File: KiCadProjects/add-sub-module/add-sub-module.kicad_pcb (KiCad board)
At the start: 2 copper layers, 0 parts

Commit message: Finished add-sub schematic
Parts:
- added U1: CD74HCT10E, footprints.pretty3:N14, F.Cu at (127.2, 108.5)
- added U2: SN74HCT00N, footprints.pretty6:N14, F.Cu at (137.8, 108.5)
- added U3: SN74HCT02N, footprints.pretty7:N14, F.Cu at (148.3, 108.5)
- added U4: SN74HCT257N, footprints.pretty8:N16, F.Cu at (158.9, 109.8)
- added U5: CD74HCT04E, footprints.pretty1:N14, F.Cu at (169.5, 108.5)

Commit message: rev. v1 for add sub
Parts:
- added C1: 0.1 uF, Capacitor_THT:C_Disc_D4.7mm_W2.5mm_P5.00mm, F.Cu at (147.0, 68.5)
- added C2: 0.1 uF, Capacitor_THT:C_Disc_D4.7mm_W2.5mm_P5.00mm, F.Cu at (147.0, 73.5)
- added C3: 0.1 uF, Capacitor_THT:C_Disc_D4.7mm_W2.5mm_P5.00mm, F.Cu at (147.0, 78.5)
- added C4: 0.1 uF, Capacitor_THT:C_Disc_D4.7mm_W2.5mm_P5.00mm, F.Cu at (147.0, 115.5)
- added C5: 0.1 uF, Capacitor_THT:C_Disc_D4.7mm_W2.5mm_P5.00mm, F.Cu at (147.0, 120.5)
- added D1: D, LED_THT:LED_D5.0mm, F.Cu at (108.7, 106.9)
- added D2: D, LED_THT:LED_D5.0mm, F.Cu at (108.7, 84.9)
- added D3: D, LED_THT:LED_D5.0mm, F.Cu at (108.7, 74.4)
- added D4: D, LED_THT:LED_D5.0mm, F.Cu at (108.7, 117.4)
- added D5: D, LED_THT:LED_D5.0mm, F.Cu at (148.2, 89.5)
- added D6: D, LED_THT:LED_D5.0mm, F.Cu at (148.2, 102.5)
- added G***: LOGO, 0_add_sub:empire, B.Cu at (113.5, 95.5)
- added J1: 2x4_Header, 0_add_sub:2x4_Header, F.Cu at (103.7, 91.7)
- added J2: 1x2_Header, 0_add_sub:1x2_Header, F.Cu at (149.5, 94.7)
- added R1: 1k, Resistor_THT:R_Axial_DIN0207_L6.3mm_D2.5mm_P7.62mm_Horizontal, F.Cu at (103.5, 102.9)
- added R2: 1k, Resistor_THT:R_Axial_DIN0207_L6.3mm_D2.5mm_P7.62mm_Horizontal, F.Cu at (103.5, 88.2)
- added R3: 1k, Resistor_THT:R_Axial_DIN0207_L6.3mm_D2.5mm_P7.62mm_Horizontal, F.Cu at (103.5, 77.9)
- added R4: 1k, Resistor_THT:R_Axial_DIN0207_L6.3mm_D2.5mm_P7.62mm_Horizontal, F.Cu at (103.5, 113.4)
- added R5: 1k, Resistor_THT:R_Axial_DIN0207_L6.3mm_D2.5mm_P7.62mm_Horizontal, F.Cu at (145.7, 83.0)
- added R6: 1k, Resistor_THT:R_Axial_DIN0207_L6.3mm_D2.5mm_P7.62mm_Horizontal, F.Cu at (145.7, 110.5)
- added REF**: MountingHole_2.2mm_M2_Pad, MountingHole:MountingHole_2.2mm_M2_Pad, F.Cu at (152.5, 64.5)
- added REF**: logo, 0_add_sub:logo, F.Cu at (123.4, 116.0)
- added REF**: MountingHole_2.2mm_M2_Pad, MountingHole:MountingHole_2.2mm_M2_Pad, F.Cu at (102.5, 126.5)
- added REF**: MountingHole_2.2mm_M2_Pad, MountingHole:MountingHole_2.2mm_M2_Pad, F.Cu at (152.5, 126.5)
- added REF**: MountingHole_2.2mm_M2_Pad, MountingHole:MountingHole_2.2mm_M2_Pad, F.Cu at (102.5, 64.5)
- added REF**: logo, 0_add_sub:logo, B.Cu at (123.4, 116.0)
- added REF**: hurd_mark, 0_add_sub:hurd_mark, B.Cu at (112.0, 67.5)
- U1: footprint footprints.pretty3:N14 -> 0_add_sub:DIP_14
- U2: footprint footprints.pretty6:N14 -> 0_add_sub:DIP_14
- U3: footprint footprints.pretty7:N14 -> 0_add_sub:DIP_14
- U4: footprint footprints.pretty8:N16 -> 0_add_sub:DIP_16
- U5: footprint footprints.pretty1:N14 -> 0_add_sub:DIP_14
- moved U5 30.8 mm to (139.1, 103.2)
- moved U3 28.9 mm to (139.1, 81.2)
- moved U1 27.3 mm to (127.1, 81.2)
- moved U4 25.9 mm to (139.1, 126.5)
- moved U2 11.9 mm to (127.1, 103.2)
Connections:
- U1 pad 7: unconnected-(U1-GND-Pad7) -> GND
- U2 pad 3: S -> SUM
- U2 pad 7: unconnected-(U2-GND-Pad7) -> GND
- U3 pad 7: unconnected-(U3-GND-Pad7) -> GND
- U4 pad 1: ~A/S -> ADD/SUB
- U4 pad 10: unconnected-(U4-3B-Pad10) -> GND
- U4 pad 11: unconnected-(U4-3A-Pad11) -> GND
- U4 pad 15: unconnected-(U4-*OE-Pad15) -> +5V
- U4 pad 5: unconnected-(U4-2A-Pad5) -> GND
- U4 pad 6: unconnected-(U4-2B-Pad6) -> GND
- U4 pad 8: unconnected-(U4-GND-Pad8) -> GND
- U5 pad 1: Cin -> CARRY
- U5 pad 12: Cout -> COUT
- U5 pad 3: Y -> KA
- U5 pad 5: X -> CA
- U5 pad 7: unconnected-(U5-GND-Pad7) -> GND
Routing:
- net +5V: track 0.00 -> 184.4 mm
- net Net-(U3-1Y): track 0.00 -> 96.6 mm
- net Net-(U1-2B): track 0.00 -> 82.7 mm, vias 0 -> 2
- net Net-(U1-1B): track 0.00 -> 66.4 mm, vias 0 -> 1
- net Net-(U1-1A): track 0.00 -> 65.5 mm, vias 0 -> 1
- net Net-(U3-4Y): track 0.00 -> 51.9 mm
- net Net-(U3-2A): track 0.00 -> 48.8 mm, vias 0 -> 1
- net CARRY: track 0.00 -> 47.4 mm, vias 0 -> 5
- net CA: track 0.00 -> 47.0 mm
- net Net-(U1-2A): track 0.00 -> 46.0 mm
- net SUM: track 0.00 -> 46.0 mm, vias 0 -> 1
- net ADD/SUB: track 0.00 -> 44.6 mm
- net Net-(U3-2B): track 0.00 -> 42.5 mm, vias 0 -> 1
- net KA: track 0.00 -> 40.6 mm, vias 0 -> 3
- net Net-(U1-3Y): track 0.00 -> 37.2 mm
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- added copper zone on B.Cu, net GND
- added copper zone on F.Cu, net GND
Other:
- board outline added: 56 x 68 mm
- board text added: "Adder-Subtractor Module"
- board text added: "Design by: Peter Hurd"
- board text added: "JLCSLCSLCS"
- board text added: "MUX 2-1"
- board text added: "NAND 2CH"
- board text added: "NAND 3CH"
- board text added: "NOR 2CH"
- board text added: "NOT 1CH"
- board text added: "Rev v.1"

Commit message: final rev v.1
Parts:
- J1: value 2x4_Header -> TSW-104-07-G-D_SAI
- J2: value 1x2_Header -> TSW-102-23-G-S_SAI
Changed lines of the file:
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@@
 			)
 		)
-		(property "Value" "1x2_Header"
+		(property "Value" "TSW-102-23-G-S_SAI"
 			(at 1.27 0 -90)
 			(unlocked yes)
@@
 			(pintype "unspecified")
 		)
+		(model "C:/projects/sdmay25-29/KiCadProjects/parts/footprints/headers/1x2_Header.step"
+			(offset
+				(xyz 0 0 0)
+			)
+			(scale
+				(xyz 1 1 1)
+			)
+			(rotate
+				(xyz 0 0 0)
+			)
+		)
 	)
 	(footprint "Resistor_THT:R_Axial_DIN0207_L6.3mm_D2.5mm_P7.62mm_Horizontal"
@@
 			(layer "F.Fab")
 		)
-		(fp_text user "*"
-			(at -7.62 -19.1897 0)
-			(unlocked yes)
-			(layer "F.SilkS")
-			(hide yes)
-			(effects
-				(font
-					(size 1 1)
-					(thickness 0.15)
-				)
-			)
-		)
-		(fp_text user "*"
-			(at -6.12 -17.5 0)
-			(layer "F.SilkS")
-			(effects
-				(font
-					(size 1 1)
-					(thickness 0.15)
-				)
-			)
-		)
 		(fp_text user "${REFERENCE}"
 			(at -3.81 -8.89 0)
@@
 			)
 		)
-		(fp_text user "*"
-			(at -7.62 -19.1897 0)
-			(unlocked yes)
-			(layer "F.Fab")
-			(effects
-				(font
-					(size 1 1)
-					(thickness 0.15)
-				)
-			)
-		)
 		(pad "1" thru_hole rect
 			(at -7.62 -17.78)
@@
 			(pintype "power_in")
 		)
-		(model "C:/projects/sdmay25-29/KiCadProjects/parts/footprints/chips/DIP_16/DIP_16.step"
+		(model "C:/projects/sdmay25-29/KiCadProjects/parts/footprints/chips/DIP_16/DIP_16.stp"
 			(offset
 				(xyz -3.75 9 2.5)
@@
 			)
 			(rotate
-				(xyz 0 0 180)
+				(xyz -90 0 0)
 			)
 		)
@@
 			)
 		)
-		(fp_text user "*"
-			(at -7.62 -16.6497 0)
-			(layer "F.SilkS")
-			(effects
-				(font
-					(size 1 1)
-					(thickness 0.15)
-				)
-			)
-		)
-		(fp_text user "*"
-			(at -7.62 -16.6497 0)
+		(fp_text user "${REFERENCE}"
+			(at -3.81 -7.62 0)
 			(unlocked yes)
 			(layer "F.Fab")
@@
 			)
 		)
-		(fp_text user "${REFERENCE}"
-			(at -3.81 -7.62 0)
-			(unlocked yes)
-			(layer "F.Fab")
-			(effects
-				(font
-					(size 1 1)
-					(thickness 0.15)
-				)
-			)
-		)
 		(pad "1" thru_hole rect
 			(at -7.62 -15.24)
@@
 			(pintype "power_in")
 		)
-		(model "C:/projects/sdmay25-29/KiCadProjects/parts/footprints/chips/DIP_14/DIP_14.step"
+		(model "C:/projects/sdmay25-29/KiCadProjects/parts/footprints/chips/DIP_14/DIP_14.stp"
 			(offset
 				(xyz -3.75 7.5 2.5)
@@
 			)
 			(rotate
-				(xyz 0 0 180)
+				(xyz -90 0 0)
 			)
 		)
@@
 			)
 		)
-		(fp_text user "*"
-			(at -7.62 -16.6497 0)
-			(layer "F.SilkS")
-			(effects
-				(font
-					(size 1 1)
-					(thickness 0.15)
-				)
-			)
-		)
-		(fp_text user "*"
-			(at -7.62 -16.6497 0)
+		(fp_text user "${REFERENCE}"
+			(at -3.81 -7.62 0)
 			(unlocked yes)
 			(layer "F.Fab")
@@
 			)
 		)
-		(fp_text user "${REFERENCE}"
-			(at -3.81 -7.62 0)
-			(unlocked yes)
-			(layer "F.Fab")
-			(effects
-				(font
-					(size 1 1)
-					(thickness 0.15)
-				)
-			)
-		)
 		(pad "1" thru_hole rect
 			(at -7.62 -15.24)
@@
 			(pintype "power_in")
 		)
-		(model "C:/projects/sdmay25-29/KiCadProjects/parts/footprints/chips/DIP_14/DIP_14.step"
+		(model "C:/projects/sdmay25-29/KiCadProjects/parts/footprints/chips/DIP_14/DIP_14.stp"
 			(offset
 				(xyz -3.75 7.5 2.5)
@@
 			)
 			(rotate
-				(xyz 0 0 180)
+				(xyz -90 0 0)
 			)
 		)
@@
 			)
 		)
-		(fp_text user "*"
-			(at -7.62 -16.6497 0)
-			(layer "F.SilkS")
-			(effects
-				(font
-					(size 1 1)
-					(thickness 0.15)
-				)
-			)
-		)
-		(fp_text user "*"
-			(at -7.62 -16.6497 0)
-			(unlocked yes)
-			(layer "F.Fab")
-			(effects
-				(font
-					(size 1 1)
-					(thickness 0.15)
-				)
-			)
-		)
 		(fp_text user "${REFERENCE}"
 			(at -3.81 -7.62 0)
@@
 			(pintype "power_in")
 		)
-		(model "C:/projects/sdmay25-29/KiCadProjects/parts/footprints/chips/DIP_14/DIP_14.step"
+		(model "C:/projects/sdmay25-29/KiCadProjects/parts/footprints/chips/DIP_14/DIP_14.stp"
 			(offset
 				(xyz -3.75 7.5 2.5)
@@
 			)
 			(rotate
-				(xyz 0 0 180)
+				(xyz -90 0 0)
 			)
 		)
@@
 		(fp_text user "*"
 			(at -7.62 -16.6497 0)
-			(layer "F.SilkS")
-			(effects
-				(font
-					(size 1 1)
-					(thickness 0.15)
-				)
-			)
-		)
-		(fp_text user "${REFERENCE}"
-			(at -3.81 -7.62 0)
-			(unlocked yes)
-			(layer "F.Fab")
-			(effects
-				(font
-					(size 1 1)
-					(thickness 0.15)
-				)
-			)
-		)
-		(fp_text user "*"
-			(at -7.62 -16.6497 0)
 			(unlocked yes)
 			(layer "F.Fab")
@@
 			)
 		)
-		(fp_text user "*"
-			(at -7.62 -16.6497 0)
+		(fp_text user "${REFERENCE}"
+			(at -3.81 -7.62 0)
 			(unlocked yes)
 			(layer "F.Fab")
@@
 			(pintype "power_in")
 		)
-		(model "C:/projects/sdmay25-29/KiCadProjects/parts/footprints/chips/DIP_14/DIP_14.step"
+		(model "C:/projects/sdmay25-29/KiCadProjects/parts/footprints/chips/DIP_14/DIP_14.stp"
 			(offset
 				(xyz -3.75 7.5 2.5)
@@
 			)
 			(rotate
-				(xyz 0 0 180)
+				(xyz -90 0 0)
 			)
 		)
@@
 			)
 		)
-		(property "Value" "2x4_Header"
+		(property "Value" "TSW-104-07-G-D_SAI"
 			(at 3.81 -1.27 -90)
 			(unlocked yes)
@@
 			(pintype "unspecified")
 		)
+		(model "C:/projects/sdmay25-29/KiCadProjects/parts/footprints/headers/2x4_Header.step"
+			(offset
+				(xyz 0 2.5 0)
+			)
+			(scale
+				(xyz 1 1 1)
+			)
+			(rotate
+				(xyz 0 0 0)
+			)
+		)
 	)

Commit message: added additional footprints to general footprint library
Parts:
- C1, C2, C3, C4, C5: footprint Capacitor_THT:C_Disc_D4.7mm_W2.5mm_P5.00mm -> 0_add_sub:C_Disc_D4.7mm_W2.5mm_P5.00mm
- D1, D2, D3, D4, D5, D6: footprint LED_THT:LED_D5.0mm -> 0_add_sub:LED_D5.0mm
- J1: value TSW-104-07-G-D_SAI -> 2x4_Header
- J2: value TSW-102-23-G-S_SAI -> 2x4_Header
- R1, R2, R3, R4, R5, R6: footprint Resistor_THT:R_Axial_DIN0207_L6.3mm_D2.5mm_P7.62mm_Horizontal -> 0_add_sub:R_Axial_DIN0207_L6.3mm_D2.5mm_P7.62mm_Horizontal

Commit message: finished tester design
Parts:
- ADD/SUB: renamed from D4; footprint 0_add_sub:LED_D5.0mm -> LED_THT:LED_D5.0mm
- C1, C2, C3, C4, C5: footprint 0_add_sub:C_Disc_D4.7mm_W2.5mm_P5.00mm -> Capacitor_THT:C_Disc_D4.7mm_W2.5mm_P5.00mm
- CA: renamed from D3; footprint 0_add_sub:LED_D5.0mm -> LED_THT:LED_D5.0mm
- CARRY: renamed from D1; footprint 0_add_sub:LED_D5.0mm -> LED_THT:LED_D5.0mm
- COUT: renamed from D6; footprint 0_add_sub:LED_D5.0mm -> LED_THT:LED_D5.0mm
- J1: moved to B.Cu
- J2: value 2x4_Header -> 1x2_Header; moved to B.Cu
- KA: renamed from D2; footprint 0_add_sub:LED_D5.0mm -> LED_THT:LED_D5.0mm
- R1, R2, R3, R4, R5, R6: footprint 0_add_sub:R_Axial_DIN0207_L6.3mm_D2.5mm_P7.62mm_Horizontal -> Resistor_THT:R_Axial_DIN0207_L6.3mm_D2.5mm_P7.62mm_Horizontal
- SUM: renamed from D5; footprint 0_add_sub:LED_D5.0mm -> LED_THT:LED_D5.0mm
- moved J1 2.52 mm to (106.3, 91.7)
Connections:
- J1 pad 1: +5V -> KA
- J1 pad 2: KA -> +5V
- J1 pad 3: RST -> CA
- J1 pad 4: CA -> RST
- J1 pad 5: CLK -> ADD/SUB
- J1 pad 6: ADD/SUB -> CLK
- J1 pad 7: GND -> CARRY
- J1 pad 8: CARRY -> GND

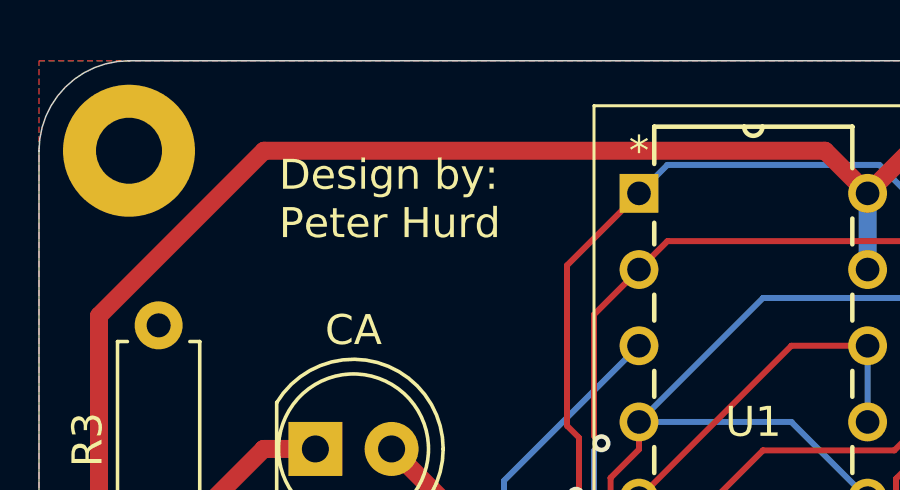
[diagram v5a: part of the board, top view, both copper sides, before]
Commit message: Updated links and footprints in add-subtractor schematic, also added my maker's mark
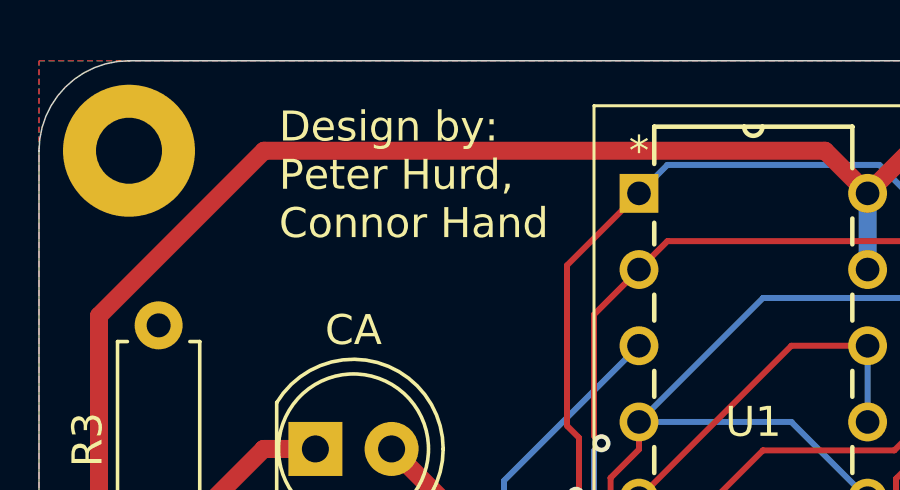
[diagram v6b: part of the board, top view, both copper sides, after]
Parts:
- removed the G*** at (113.5, 95.5)
- added G***: LOGO, 0_add_sub:hand_mark, B.Cu at (115.5, 73.0)
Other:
- board text added: "Design by: Peter Hurd, Connor Hand"
- board text removed: "Design by: Peter Hurd"

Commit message: still need to fix traces
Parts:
- J1: footprint 0_add_sub:2x4_Header -> Connector_PinHeader_2.54mm:PinHeader_2x04_P2.54mm_Vertical
- J2: footprint 0_add_sub:1x2_Header -> Connector_PinHeader_2.54mm:PinHeader_1x02_P2.54mm_Vertical
- MUX 2-1: renamed from U4; footprint 0_add_sub:DIP_16 -> Package_DIP:DIP-16_W7.62mm_Socket
- NAND 2CH: renamed from U2; footprint 0_add_sub:DIP_14 -> Package_DIP:DIP-14_W7.62mm_Socket
- NAND 3CH: renamed from U1; footprint 0_add_sub:DIP_14 -> Package_DIP:DIP-14_W7.62mm_Socket
- NOR 2CH: renamed from U3; footprint 0_add_sub:DIP_14 -> Package_DIP:DIP-14_W7.62mm_Socket
- NOT 1CH: renamed from U5; footprint 0_add_sub:DIP_14 -> Package_DIP:DIP-14_W7.62mm_Socket
- moved MUX 2-1 19.5 mm to (131.5, 108.5)
- moved NAND 3CH 17.0 mm to (119.5, 65.9)
- moved NOR 2CH 17.0 mm to (131.5, 65.9)
- moved NOT 1CH 17.0 mm to (131.5, 87.9)
- moved NAND 2CH 17.0 mm to (119.5, 88.0)
- turned J1 to 180 degrees
- turned J2 to 180 degrees
- renumbered CARRY to D1, KA to D2, CA to D3, ADD/SUB to D4, SUM to D5, COUT to D6
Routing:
- net Net-(U1-1A): track 65.5 -> 71.7 mm
- net Net-(U3-1Y): track 96.6 -> 95.8 mm
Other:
- board text added: "JLCJLCJLCJLC"
- board text added: "Licensed under CERN-OHL-P v2"
- board text added: "Rev. A"
- board text added: "SDMAY25-29"
- board text removed: "JLCSLCSLCS"
- board text removed: "MUX 2-1"
- board text removed: "NAND 2CH"
- board text removed: "NAND 3CH"
- board text removed: "NOR 2CH"
- board text removed: "NOT 1CH"
- board text removed: "Rev v.1"

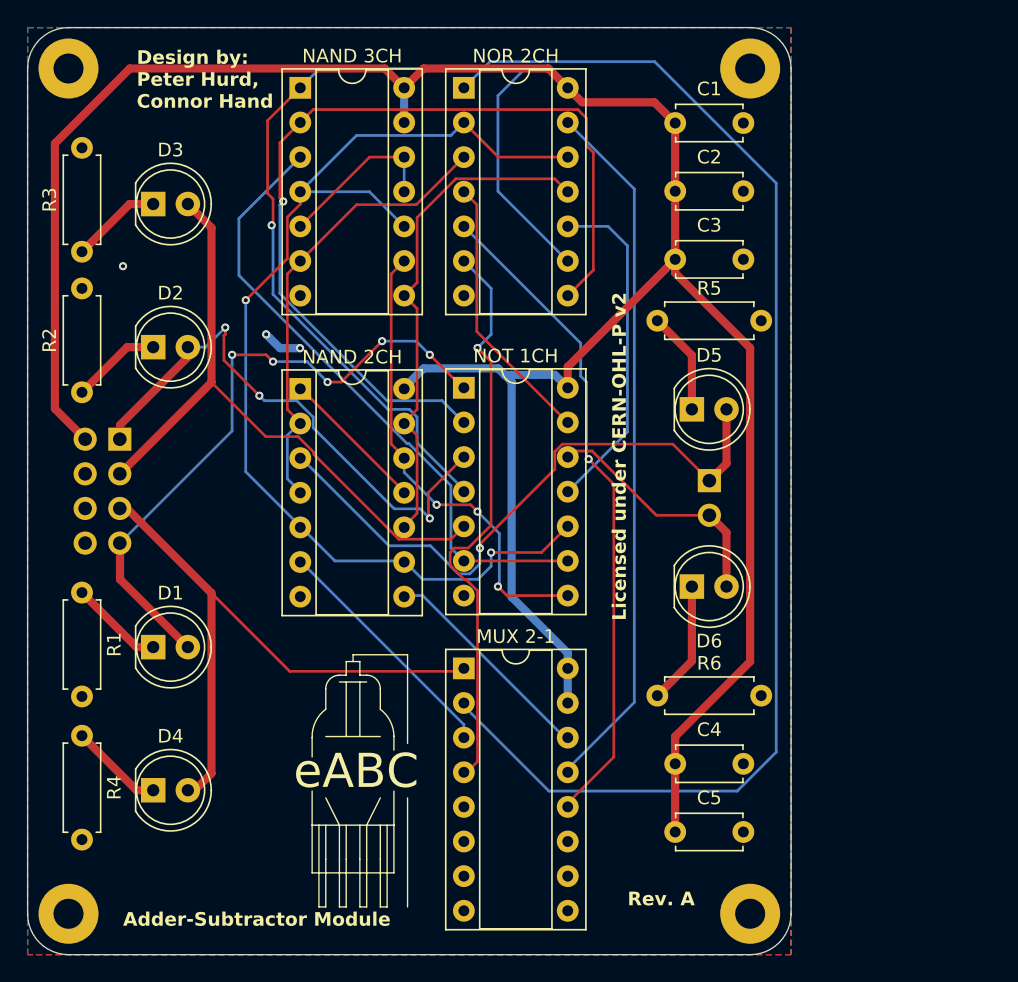
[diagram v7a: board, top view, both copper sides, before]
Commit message: fixed module, need work on tester
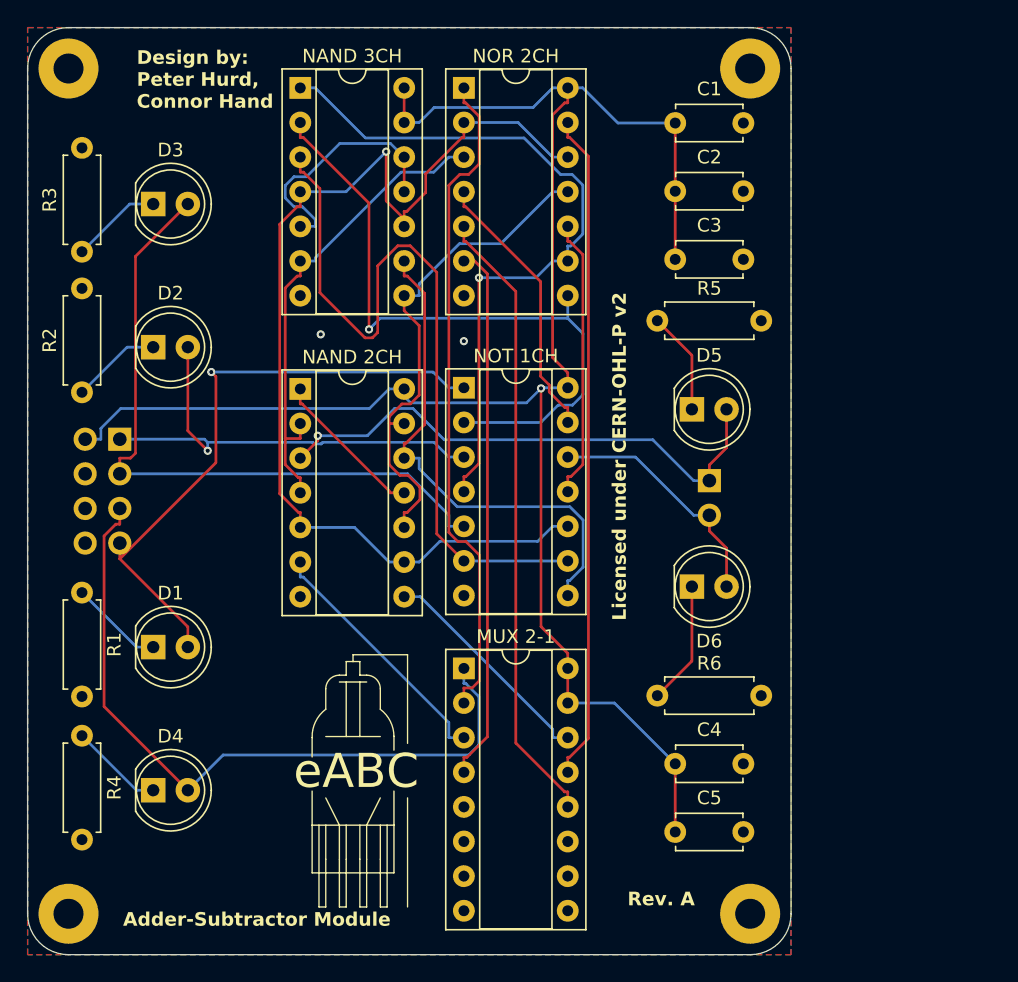
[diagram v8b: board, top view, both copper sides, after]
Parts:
- renumbered REF** to Logo1, REF** to Logo2, REF** to M1, REF** to M2, REF** to M3, REF** to M4
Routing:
- net +5V: track 184.4 -> 135.0 mm, vias 0 -> 1
- net Net-(U3-1Y): track 95.8 -> 49.1 mm
- net Net-(U1-1A): track 71.7 -> 53.1 mm
- net Net-(U1-1B): track 66.4 -> 49.6 mm
- net Net-(U1-2A): track 46.0 -> 56.7 mm
- net ADD/SUB: track 44.6 -> 52.7 mm
- net SUM: track 46.0 -> 39.7 mm
- net Net-(U1-1Y): track 12.3 -> 18.3 mm
- net KA: track 40.6 -> 34.7 mm, vias 3 -> 1
- net Net-(U3-3Y): track 24.8 -> 20.6 mm
- net Net-(U1-2B): track 82.7 -> 79.1 mm, vias 2 -> 1
- net Net-(U1-3A): track 34.5 -> 37.5 mm, vias 3 -> 0
- net Net-(U3-2B): track 42.5 -> 39.5 mm, vias 1 -> 0
- net GND: track 2.91 -> 0.00 mm, vias 3 -> 2
- net Net-(U3-4Y): track 51.9 -> 49.1 mm
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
